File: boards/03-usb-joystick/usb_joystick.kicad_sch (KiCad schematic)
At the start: 12 parts, among them J1 USB-C, J2 Joystick, SW1 Button, SW2 Button, SW3 Button, SW4 Button, U1 MCU, Y1 16MHz

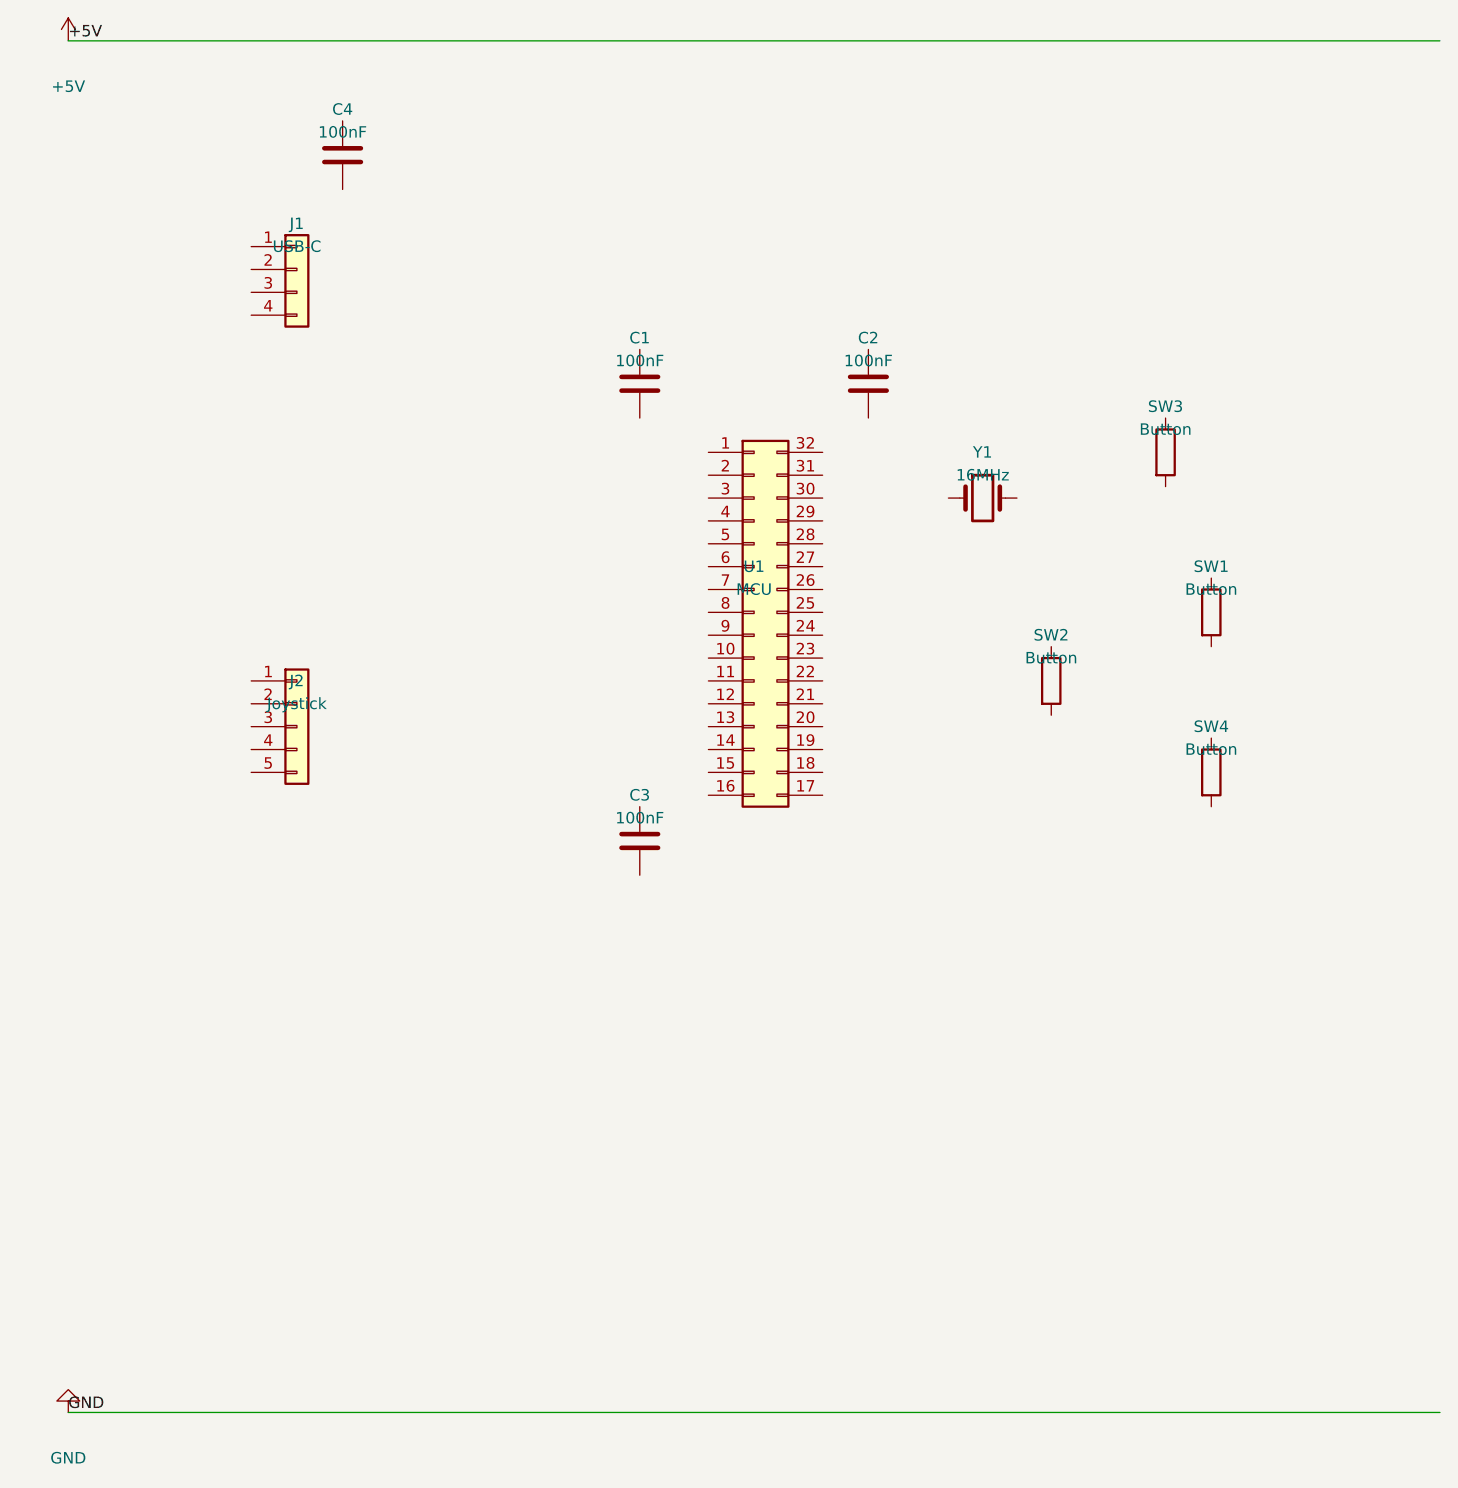
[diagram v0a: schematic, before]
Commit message: fix(boards): Add signal wiring to USB joystick schematic generator
Add comprehensive signal wiring using global labels (same pattern as
charlieplex demo) to connect all components:
- USB connector pins (D+, D-, VCC, GND) to MCU
- Joystick connector pins (X, Y, button) to MCU ADC/GPIO
- Crystal pins to MCU XTAL pins
- Button pins to MCU GPIO with GND connections
- Decoupling capacitors between VCC and GND
- No-connect markers on unused MCU pins

The schematic now has 44 wires and 44 global labels for proper
connectivity, compared to only 2 power rail wires before.

Co-Authored-By: Claude Opus 4.5 <noreply@anthropic.com>
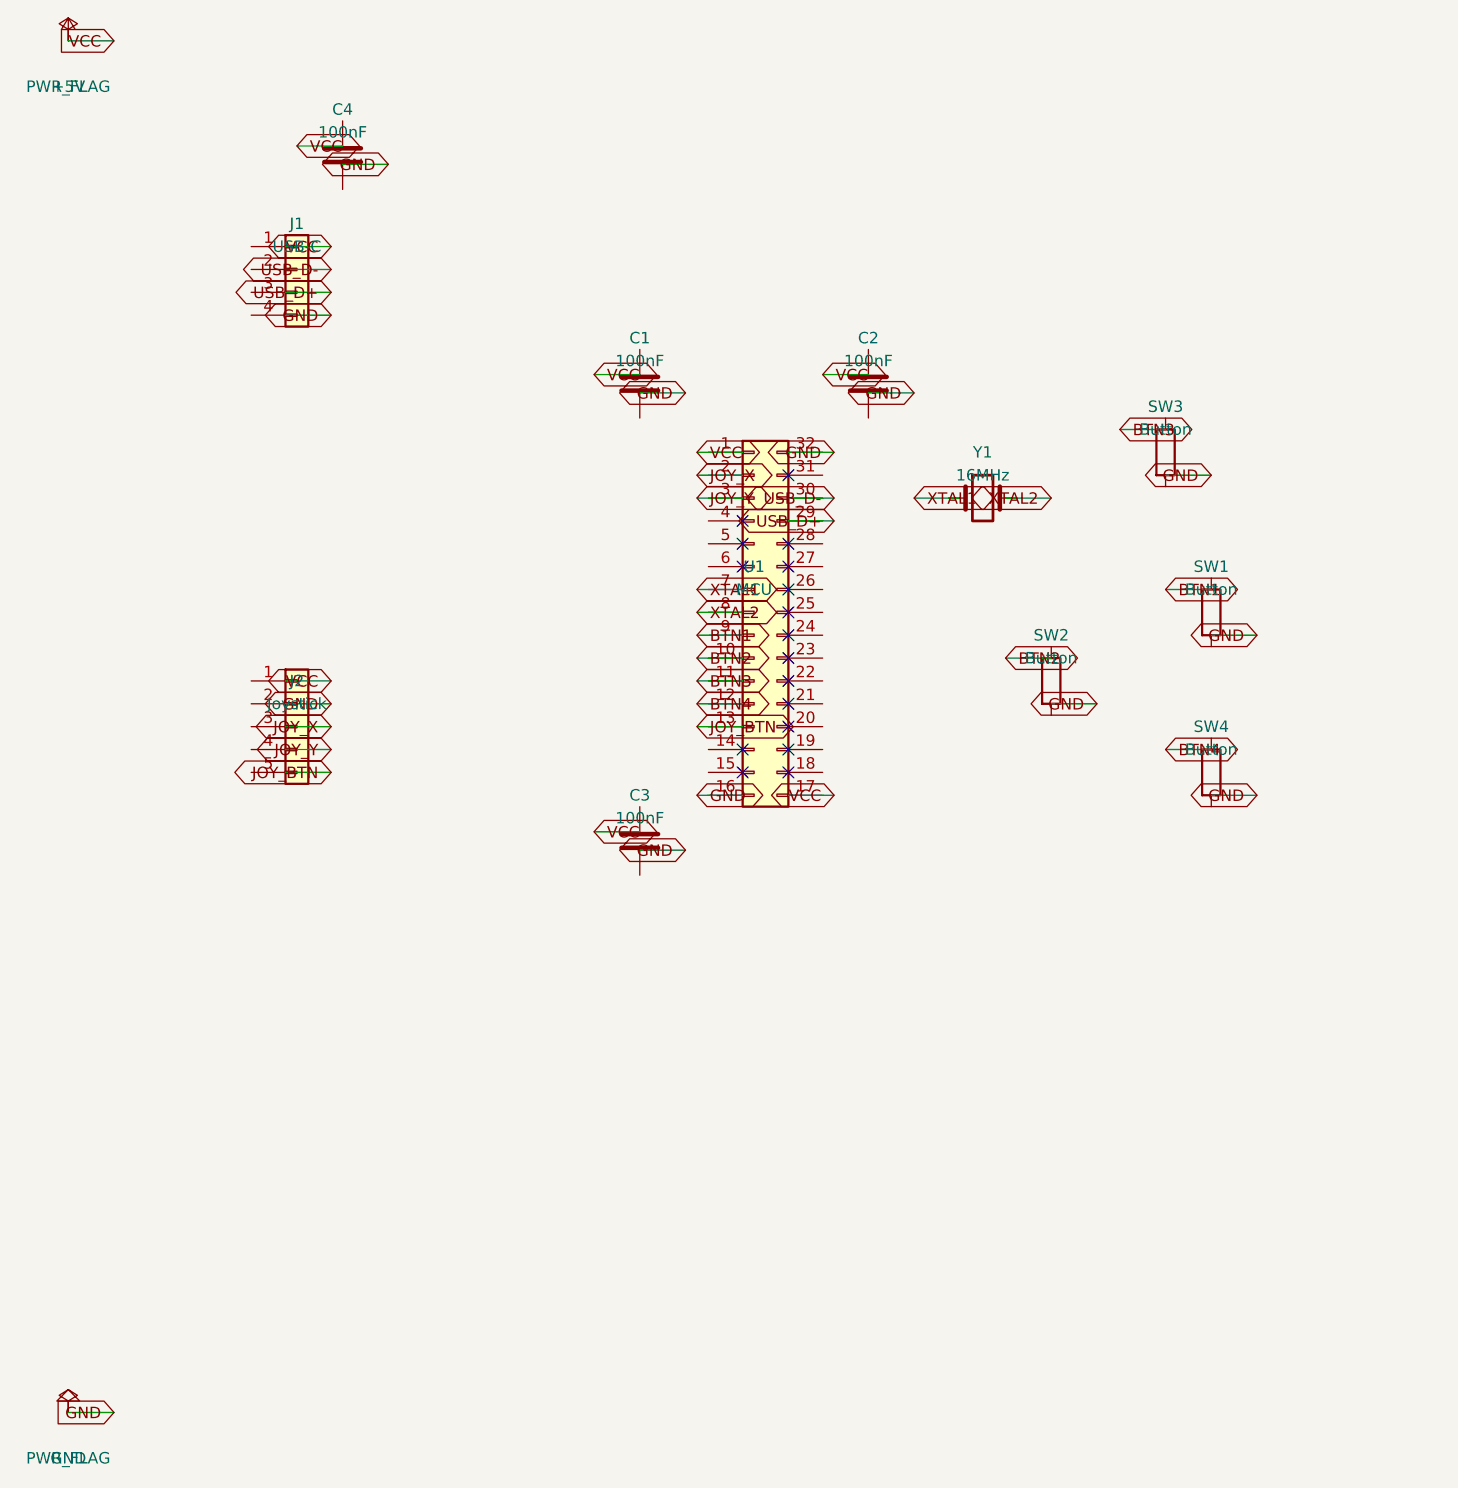
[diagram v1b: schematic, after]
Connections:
- no-connect marks 0 -> 17

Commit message: fix(schematic): Correct pin connection_point to return wire position
The Pin.connection_point() method was incorrectly calculating the wire
connection point by adding the pin length at the specified angle.
In KiCad's schematic format, the pin's (at x y angle) specifies the
endpoint where wires connect - the connection point IS the (x, y)
position directly.

This fixes ERC validation errors in demo schematics where wires
were being placed at the wrong position relative to component pins.

Regenerated demo schematics with correct wire positions.

Closes #700

Co-Authored-By: Claude Opus 4.5 <noreply@anthropic.com>
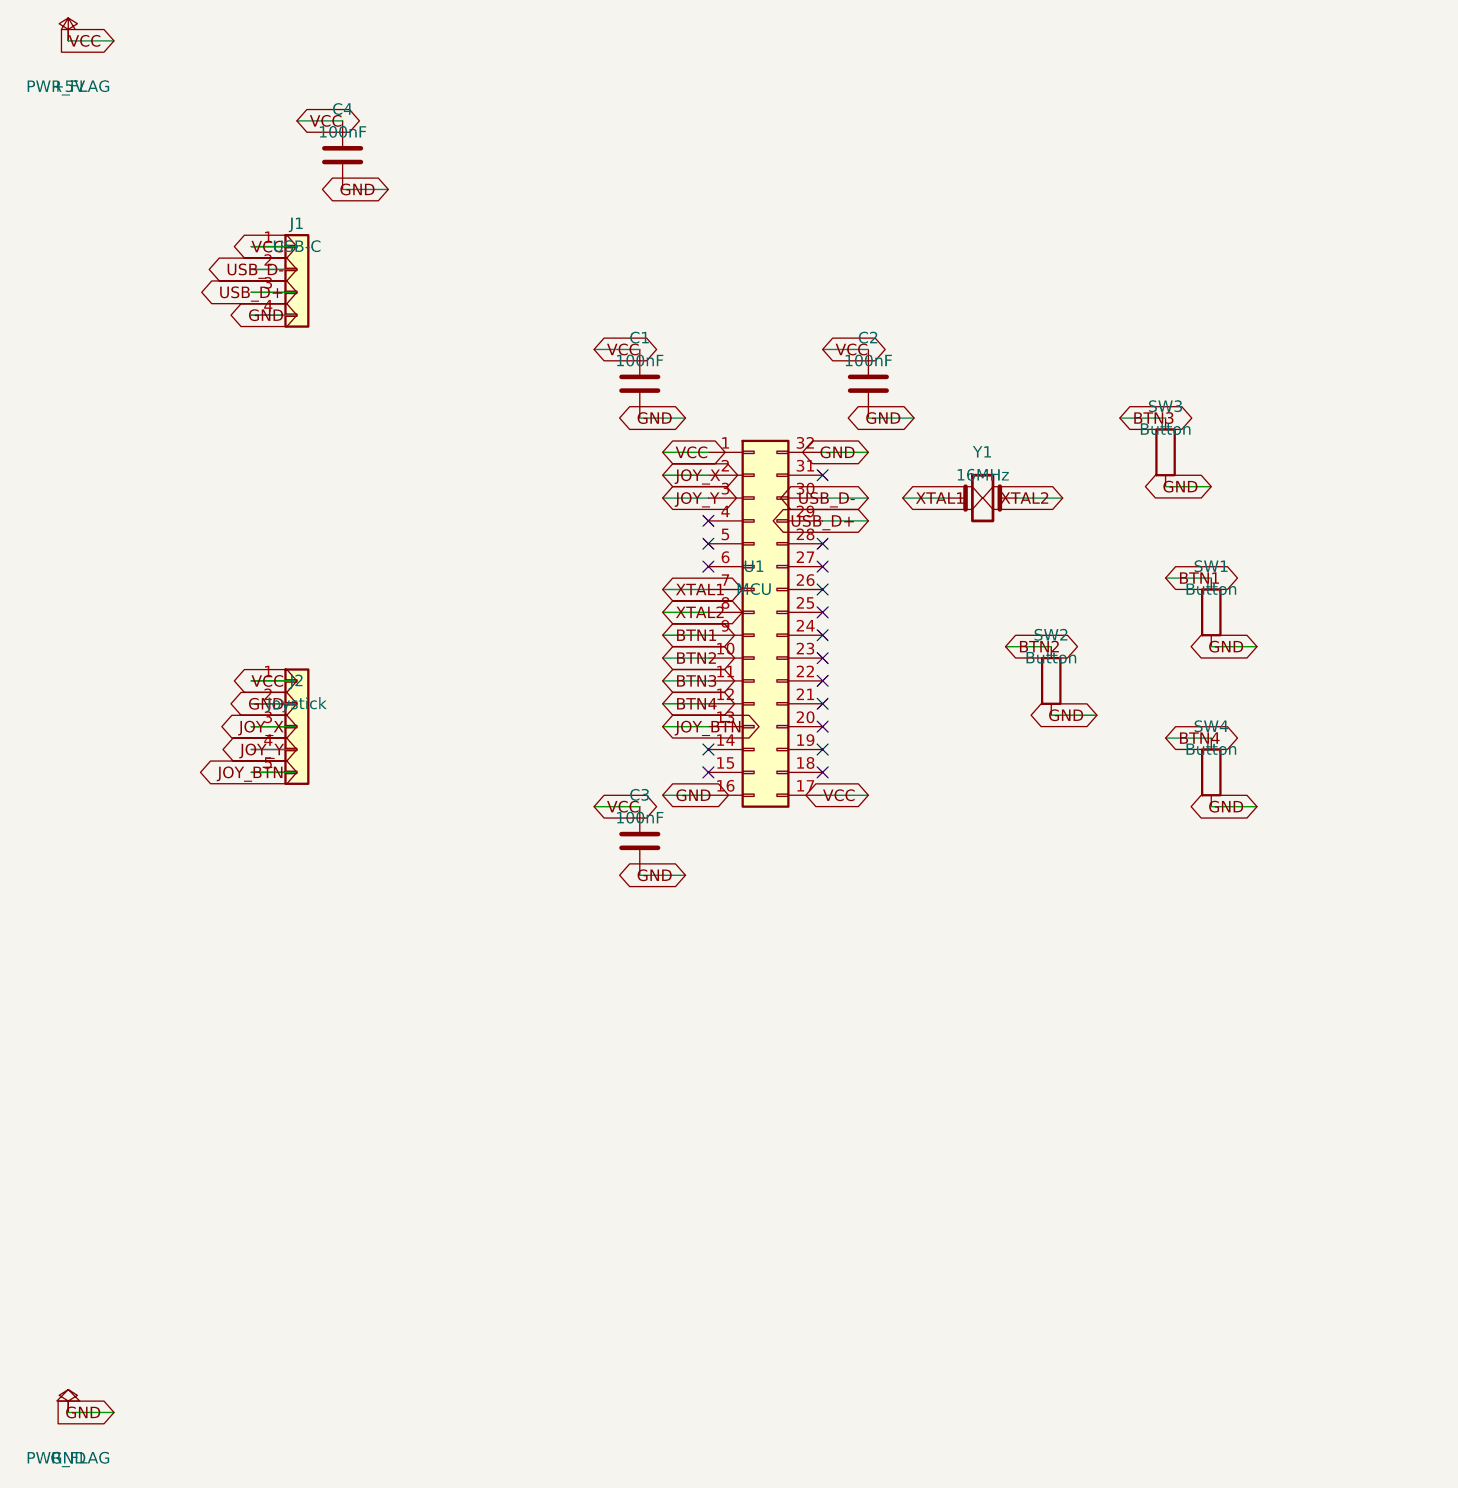
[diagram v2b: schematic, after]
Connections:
- net +5V: now also C1.1, C2.1, C3.1, C4.1, J1.1 (Pin_1), J2.1 (Pin_1), U1.1 (Pin_1), U1.17 (Pin_17)
- net BTN1: now also SW1.1, U1.9 (Pin_9)
- net BTN2: now also SW2.1, U1.10 (Pin_10)
- net BTN3: now also SW3.1, U1.11 (Pin_11)
- net BTN4: now also SW4.1, U1.12 (Pin_12)
- net GND: now also C1.2, C2.2, C3.2, C4.2, J1.4 (Pin_4), J2.2 (Pin_2), SW1.2, SW2.2, SW3.2, SW4.2, U1.16 (Pin_16), U1.32 (Pin_32)
- net JOY_BTN: now also J2.5 (Pin_5), U1.13 (Pin_13)
- net JOY_X: now also J2.3 (Pin_3), U1.2 (Pin_2)
- net JOY_Y: now also J2.4 (Pin_4), U1.3 (Pin_3)
- net USB_D+: now also J1.3 (Pin_3), U1.29 (Pin_29)
- net USB_D-: now also J1.2 (Pin_2), U1.30 (Pin_30)
- net XTAL1: now also U1.7 (Pin_7), Y1.1
- net XTAL2: now also U1.8 (Pin_8), Y1.2
